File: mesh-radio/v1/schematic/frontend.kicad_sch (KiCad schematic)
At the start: 51 parts, among them J4 U.FL-R-SMT-1(80), U11 QPA9510TR7, U12 SKY13330-397LF, U13 BGA7L1BN6E6327XTSA1

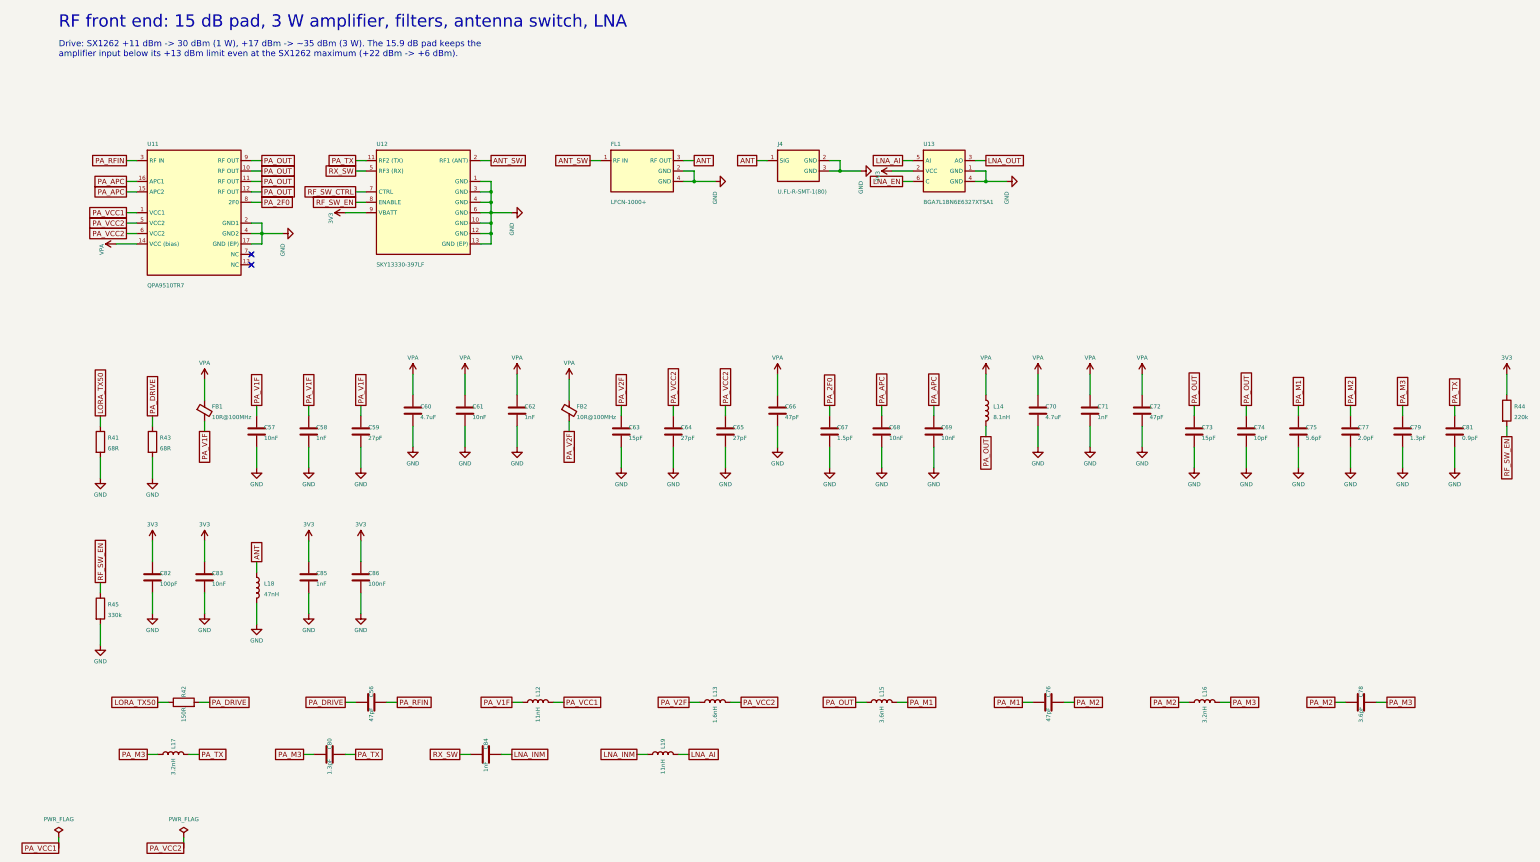
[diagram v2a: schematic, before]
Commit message: Mesh radio v1: LFCG-1000+ antenna filter; missing-antenna detector
Owner decisions of 19 Oct: keep 3 W with the heat fixes and a gap pad to
a metal enclosure, 6 layers, 300 mA charging, new parts at the designer's
judgement.  This commit, from sim/rf:
- FL1 LFCN-1000+ (1206) -> LFCG-1000+ (0805, 8 pads, Mini-Circuits case
  GE0805C-2: in 8, out 4): no stop-band re-entry at 5.5-10 GHz, where the
  3 W 6th-10th harmonics failed FCC's restricted-band limit;
- a reflected-wave detector: a printed line beside the ANT line
  terminated in 49.9 R, an Infineon BAT15-02EL, 1 nF and 100 k into
  P0.30/AIN6, so firmware can cut the amplifier within ~1 ms of a packet
  with no antenna (the antenna switch sees 109-160 % of its rating then);
- P0.31/AIN7 reads the charger's NTC (firmware's 0-45 C charging rule);
  the expansion header's IO3/IO4 give way (four spare pins remain).
ERC 0, netlist equals circuit.py, every pin and pad accounted for.

Co-Authored-By: Claude Opus 5.5 <noreply@anthropic.com>
Claude-Session: https://claude.ai/code/session_015TBB2ThqxHSgA8MkFosmn9
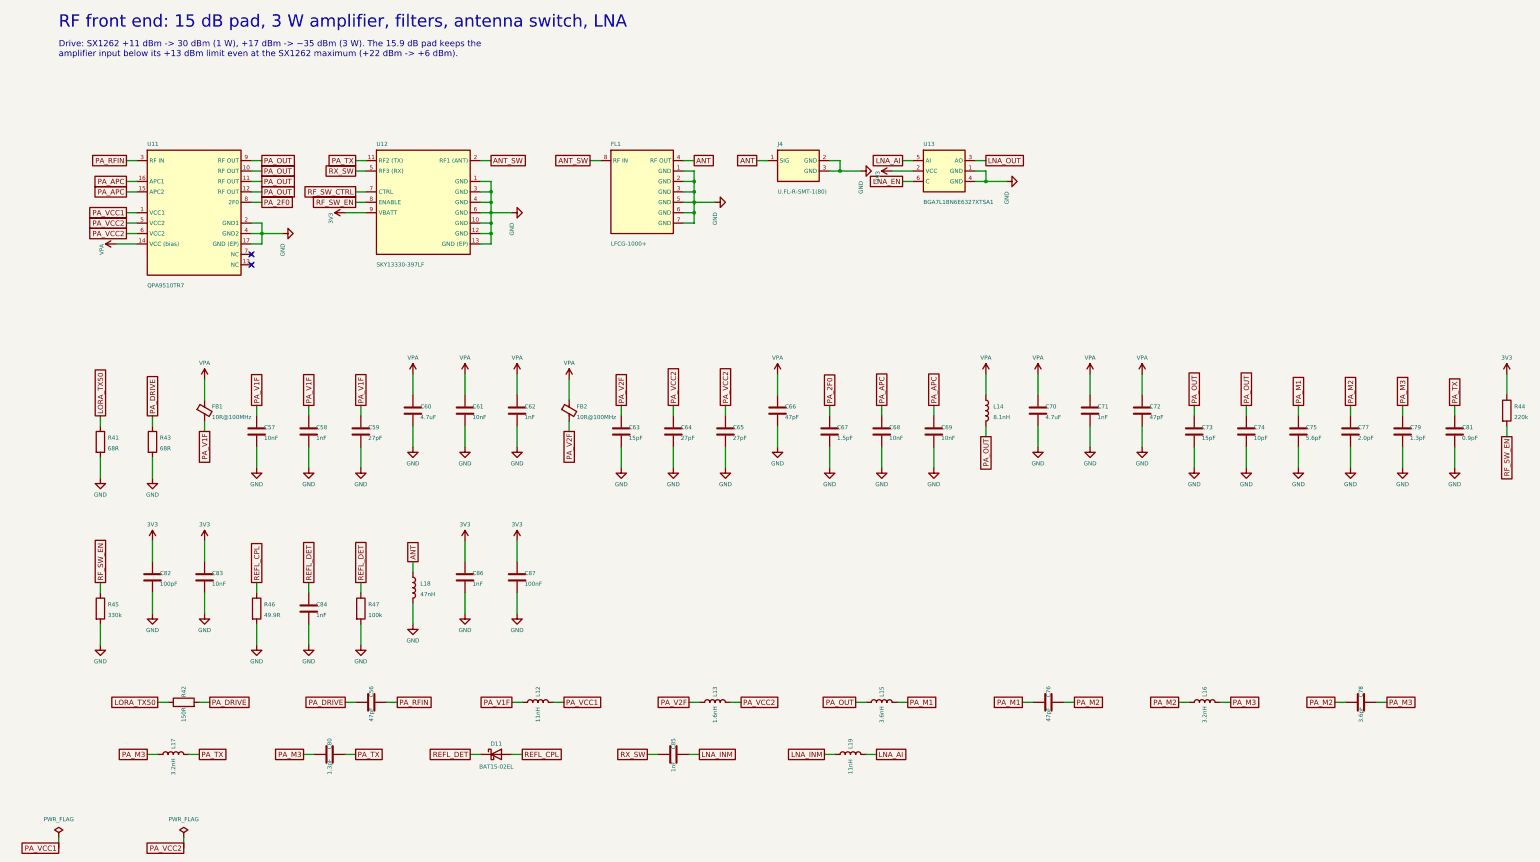
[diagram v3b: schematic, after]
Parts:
- added C87: 100nF, og:C_0402, symbol Device:C
- added D11: BAT15-02EL, og:TSLP-2-19_L1.0-W0.6-P0.65-RD, symbol og_device:D_Schottky_BAT15
- added R46: 49.9R, og:R_0402, symbol Device:R
- added R47: 100k, og:R_0402, symbol Device:R
- C77: DigiKey (none) -> 490-8124-1-ND
- C78: DigiKey (none) -> 490-8127-1-ND
- C81: DigiKey (none) -> 490-GQM1875C2ER90BB12DCT-ND
- C86: value 100nF -> 1nF; DigiKey 1276-1001-1-ND -> 490-3244-1-ND; LCSC C1525 -> C76947; MPN CL05B104KO5NNNC -> GRM1555C1H102JA01D; Manufacturer Samsung Electro-Mechanics -> Murata
- FL1: value LFCN-1000+ -> LFCG-1000+; footprint og:FILTER-SMD_1206-4P-L3.2-W1.6-L -> og:FILTER-SMD_8P-L2.0-W1.3-BL_LFCG-XX; symbol og:LFCN1000 -> og:LFCG1000; DigiKey 3157-LFCN-1000+CT-ND -> 3157-LFCG-1000+CT-ND; LCSC C879868 -> C4989745; MPN LFCN-1000+ -> LFCG-1000+
- L15: DigiKey (none) -> 490-16042-1-ND
- L16, L17: DigiKey (none) -> 490-16041-1-ND
- R41: DigiKey (none) -> 541-10549-1-ND
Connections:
- net 3V3: now also C87.1; no longer C85.1
- net ANT: now also FL1.4 (RF OUT); no longer FL1.3 (RF OUT)
- net ANT_SW: now also FL1.8 (RF IN); no longer FL1.1 (RF IN)
- net GND: now also C84.2, FL1.1 (GND), FL1.3 (GND), FL1.5 (GND), FL1.6 (GND), FL1.7 (GND), C87.2, R46.2, R47.2; no longer C85.2, FL1.4 (GND)
- net LNA_INM: now also C85.2; no longer C84.2
- net RX_SW: now also C85.1; no longer C84.1
- new net REFL_CPL: D11.2 (A), R46.1
- new net REFL_DET: C84.1, D11.1 (K), R47.1
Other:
- moved on the sheet: C84, C85, C86, L18, L19

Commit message: Mesh radio v1: power-path and firmware rework in progress (snapshot)
Co-Authored-By: Claude Opus 5.5 <noreply@anthropic.com>
Claude-Session: https://claude.ai/code/session_015TBB2ThqxHSgA8MkFosmn9
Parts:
- removed C86: 1nF, og:C_0402, symbol Device:C
- removed C87: 100nF, og:C_0402, symbol Device:C
- removed D11: BAT15-02EL, og:TSLP-2-19_L1.0-W0.6-P0.65-RD, symbol og_device:D_Schottky_BAT15
- removed R41, R43: 68R, og:R_0805, symbol Device:R
- removed R42: 150R, og:R_0805, symbol Device:R
- removed R44: 220k, og:R_0402, symbol Device:R
- removed R45: 330k, og:R_0402, symbol Device:R
- removed U13: BGA7L1BN6E6327XTSA1, og:TSNP-6_L1.1-W0.7-P0.40-BL, symbol og:BGA7L1BN6
- added C54: 47pF, og:C_0402, symbol Device:C
- added C55: 10nF, og:C_0402, symbol Device:C
- added D8: BAT15-02EL, og:TSLP-2-19_L1.0-W0.6-P0.65-RD, symbol og_device:D_Schottky_BAT15
- added R48: 68R, og:R_0805, symbol Device:R
- added R49: 220k, og:R_0402, symbol Device:R
- added R50: 330k, og:R_0402, symbol Device:R
- added R51: 49.9R, og:R_0402, symbol Device:R
- added R52: 100k, og:R_0402, symbol Device:R
- added U10: QPA9510TR7, og:QFN-16_3x3_QPA9510, symbol og:QPA9510
- C56: value 47pF -> 1nF; DigiKey 490-14446-1-ND -> 490-3244-1-ND; LCSC C161322 -> C76947; MPN GJM1555C1H470JB01D -> GRM1555C1H102JA01D
- C57: value 10nF -> 27pF; DigiKey 1276-1028-1-ND -> 490-17672-1-ND; LCSC C15195 -> C88884; MPN CL05B103KB5NNNC -> GJM1555C1H270JB01D; Manufacturer Samsung Electro-Mechanics -> Murata
- C58: value 1nF -> 4.7uF; footprint og:C_0402 -> og:C_0603; DigiKey 490-3244-1-ND -> 1276-1044-1-ND; LCSC C76947 -> C1705; MPN GRM1555C1H102JA01D -> CL10A475KP8NNNC; Manufacturer Murata -> Samsung Electro-Mechanics
- C59: value 27pF -> 10nF; DigiKey 490-17672-1-ND -> 1276-1028-1-ND; LCSC C88884 -> C15195; MPN GJM1555C1H270JB01D -> CL05B103KB5NNNC; Manufacturer Murata -> Samsung Electro-Mechanics
- C60: value 4.7uF -> 1nF; footprint og:C_0603 -> og:C_0402; DigiKey 1276-1044-1-ND -> 490-3244-1-ND; LCSC C1705 -> C76947; MPN CL10A475KP8NNNC -> GRM1555C1H102JA01D; Manufacturer Samsung Electro-Mechanics -> Murata
- C61: value 10nF -> 15pF; DigiKey 1276-1028-1-ND -> 490-3117-1-ND; LCSC C15195 -> C88877; MPN CL05B103KB5NNNC -> GJM1555C1H150JB01D; Manufacturer Samsung Electro-Mechanics -> Murata
- C62: value 1nF -> 27pF; DigiKey 490-3244-1-ND -> 490-17672-1-ND; LCSC C76947 -> C88884; MPN GRM1555C1H102JA01D -> GJM1555C1H270JB01D
- C63: value 15pF -> 27pF; DigiKey 490-3117-1-ND -> 490-17672-1-ND; LCSC C88877 -> C88884; MPN GJM1555C1H150JB01D -> GJM1555C1H270JB01D
- C64: value 27pF -> 47pF; DigiKey 490-17672-1-ND -> 490-14446-1-ND; LCSC C88884 -> C161322; MPN GJM1555C1H270JB01D -> GJM1555C1H470JB01D
- C65: value 27pF -> 1.5pF; DigiKey 490-17672-1-ND -> 490-8087-1-ND; LCSC C88884 -> C76900; MPN GJM1555C1H270JB01D -> GJM1555C1H1R5BB01D
- C66: value 47pF -> 10nF; DigiKey 490-14446-1-ND -> 1276-1028-1-ND; LCSC C161322 -> C15195; MPN GJM1555C1H470JB01D -> CL05B103KB5NNNC; Manufacturer Murata -> Samsung Electro-Mechanics
- C67: value 1.5pF -> 10nF; DigiKey 490-8087-1-ND -> 1276-1028-1-ND; LCSC C76900 -> C15195; MPN GJM1555C1H1R5BB01D -> CL05B103KB5NNNC; Manufacturer Murata -> Samsung Electro-Mechanics
- C68: value 10nF -> 4.7uF; footprint og:C_0402 -> og:C_0603; DigiKey 1276-1028-1-ND -> 1276-1044-1-ND; LCSC C15195 -> C1705; MPN CL05B103KB5NNNC -> CL10A475KP8NNNC
- C69, C83: value 10nF -> 1nF; DigiKey 1276-1028-1-ND -> 490-3244-1-ND; LCSC C15195 -> C76947; MPN CL05B103KB5NNNC -> GRM1555C1H102JA01D; Manufacturer Samsung Electro-Mechanics -> Murata
- C70: value 4.7uF -> 47pF; footprint og:C_0603 -> og:C_0402; DigiKey 1276-1044-1-ND -> 490-14446-1-ND; LCSC C1705 -> C161322; MPN CL10A475KP8NNNC -> GJM1555C1H470JB01D; Manufacturer Samsung Electro-Mechanics -> Murata
- C71: value 1nF -> 15pF; footprint og:C_0402 -> og:C_0603; DigiKey 490-3244-1-ND -> 490-14794-1-ND; LCSC C76947 -> C2181572; MPN GRM1555C1H102JA01D -> GQM1875C2E150JB12D
- C72: value 47pF -> 10pF; footprint og:C_0402 -> og:C_0603; DigiKey 490-14446-1-ND -> 490-6086-1-ND; LCSC C161322 -> C882554; MPN GJM1555C1H470JB01D -> GQM1875C2E100JB12D
- C73: value 15pF -> 5.6pF; DigiKey 490-14794-1-ND -> 490-7162-1-ND; LCSC C2181572 -> C2171689; MPN GQM1875C2E150JB12D -> GQM1875C2E5R6CB12D
- C74: value 10pF -> 47pF; DigiKey 490-6086-1-ND -> 490-5900-1-ND; LCSC C882554 -> C882552; MPN GQM1875C2E100JB12D -> GQM1875C2E470JB12D
- C75: value 5.6pF -> 2.0pF; DigiKey 490-7162-1-ND -> 490-8124-1-ND; LCSC C2171689 -> C6867410; MPN GQM1875C2E5R6CB12D -> GQM1875C2E2R0BB12D
- C76: value 47pF -> 3.6pF; DigiKey 490-5900-1-ND -> 490-8127-1-ND; LCSC C882552 -> C2178747; MPN GQM1875C2E470JB12D -> GQM1875C2E3R6BB12D
- C77: value 2.0pF -> 1.3pF; DigiKey 490-8124-1-ND -> (none); LCSC C6867410 -> C3901219; MPN GQM1875C2E2R0BB12D -> GQM1875C2E1R3BB12D
- C78: value 3.6pF -> 1.3pF; DigiKey 490-8127-1-ND -> (none); LCSC C2178747 -> C3901219; MPN GQM1875C2E3R6BB12D -> GQM1875C2E1R3BB12D
- C79: value 1.3pF -> 0.9pF; DigiKey (none) -> 490-GQM1875C2ER90BB12DCT-ND; LCSC C3901219 -> C1865143; MPN GQM1875C2E1R3BB12D -> GQM1875C2ER90BB12D
- C80: value 1.3pF -> 100pF; footprint og:C_0603 -> og:C_0402; DigiKey (none) -> 490-5922-1-ND; LCSC C3901219 -> C77177; MPN GQM1875C2E1R3BB12D -> GRM1555C1H101JA01D
- C81: value 0.9pF -> 10nF; footprint og:C_0603 -> og:C_0402; DigiKey 490-GQM1875C2ER90BB12DCT-ND -> 1276-1028-1-ND; LCSC C1865143 -> C15195; MPN GQM1875C2ER90BB12D -> CL05B103KB5NNNC; Manufacturer Murata -> Samsung Electro-Mechanics
- C82: value 100pF -> 1nF; DigiKey 490-5922-1-ND -> 490-3244-1-ND; LCSC C77177 -> C76947; MPN GRM1555C1H101JA01D -> GRM1555C1H102JA01D
- C85: value 1nF -> 100nF; DigiKey 490-3244-1-ND -> 1276-1001-1-ND; LCSC C76947 -> C1525; MPN GRM1555C1H102JA01D -> CL05B104KO5NNNC; Manufacturer Murata -> Samsung Electro-Mechanics
- R46: value 49.9R -> 68R; footprint og:R_0402 -> og:R_0805; DigiKey 311-49.9LRCT-ND -> 541-10549-1-ND; LCSC C87044 -> C2114866; MPN RC0402FR-0749R9L -> RCS080568R0FKEA; Manufacturer Yageo -> Vishay Dale
- R47: value 100k -> 150R; footprint og:R_0402 -> og:R_0805; DigiKey 311-100KLRCT-ND -> 311-150CRCT-ND; LCSC C60491 -> C114523; MPN RC0402FR-07100KL -> RC0805FR-07150RL
- U11: value QPA9510TR7 -> SKY13330-397LF; footprint og:QFN-16_3x3_QPA9510 -> og:QFN-12_L2.0-W2.0-P0.50-BL-EP0.8; symbol og:QPA9510 -> og:SKY13330; DigiKey 2312-QPA9510TR7CT-ND -> 863-1643-1-ND; LCSC C52059849 -> C2654715; MPN QPA9510TR7 -> SKY13330-397LF; Manufacturer Qorvo -> Skyworks Solutions
- U12: value SKY13330-397LF -> BGA7L1BN6E6327XTSA1; footprint og:QFN-12_L2.0-W2.0-P0.50-BL-EP0.8 -> og:TSNP-6_L1.1-W0.7-P0.40-BL; symbol og:SKY13330 -> og:BGA7L1BN6; DigiKey 863-1643-1-ND -> BGA7L1BN6E6327XTSA1CT-ND; LCSC C2654715 -> C534173; MPN SKY13330-397LF -> BGA7L1BN6E6327XTSA1; Manufacturer Skyworks Solutions -> Infineon Technologies
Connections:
- net 3V3: now also C80.1, C81.1, C84.1, C85.1, U11.9 (VBATT), U12.2 (VCC), R49.1; no longer C82.1, C83.1, U12.9 (VBATT)
- net ANT_SW: now also U11.2 (RF1 (ANT)); no longer U12.2 (RF1 (ANT))
- net GND: now also C56.2, C80.2, C85.2, U11.1 (GND), U11.10 (GND), U11.12 (GND), U11.13 (GND (EP)), U11.3 (GND), U11.6 (GND), C55.2, R48.2, R50.2, R51.2, R52.2, U10.17 (GND (EP)), U10.2 (GND1), U10.4 (GND2); no longer C74.2, C83.2, R47.2, U11.17 (GND (EP)), U11.2 (GND1), U12.10 (GND), U12.12 (GND), U12.13 (GND (EP)), U12.3 (GND), U12.6 (GND)
- net LNA_AI: now also U12.5 (AI)
- net LNA_EN: now also U12.6 (C)
- net LNA_INM: now also C83.2; no longer C85.2
- net LNA_OUT: now also U12.3 (AO)
- net LORA_TX50: now also R46.1, R47.1
- net PA_2F0: now also C65.1, U10.8 (2F0); no longer C67.1, U11.8 (2F0)
- net PA_APC: now also C66.1, C67.1, U10.15 (APC2), U10.16 (APC1); no longer C68.1, C69.1, U11.15 (APC2), U11.16 (APC1)
- net PA_DRIVE: now also R47.2, C54.1, R48.1; no longer C56.1
- net PA_M1: now also C73.1, C74.1; no longer C75.1, C76.1
- net PA_M2: now also C74.2, C75.1, C76.1; no longer C76.2, C77.1, C78.1
- net PA_M3: now also C76.2, C77.1, C78.1; no longer C78.2, C79.1, C80.1
- net PA_OUT: now also C71.1, C72.1, U10.10 (RF OUT), U10.11 (RF OUT), U10.12 (RF OUT), U10.9 (RF OUT); no longer C73.1, C74.1, U11.10 (RF OUT), U11.11 (RF OUT), U11.12 (RF OUT), U11.9 (RF OUT)
- net PA_RFIN: now also C54.2, U10.3 (RF IN); no longer C56.2, U11.3 (RF IN)
- net PA_TX: now also C78.2, C79.1, U11.11 (RF2 (TX)); no longer C80.2, C81.1, U12.11 (RF2 (TX))
- net PA_V1F: now also C56.1, C55.1; no longer C58.1, C59.1
- net PA_V2F: now also C61.1; no longer C63.1
- net PA_VCC1: now also U10.1 (VCC1); no longer U11.1 (VCC1)
- net PA_VCC2: now also C62.1, C63.1, U10.5 (VCC2), U10.6 (VCC2); no longer C64.1, C65.1, U11.5 (VCC2), U11.6 (VCC2)
- net REFL_CPL: now also D8.2 (A), R51.1; no longer R46.1
- net REFL_DET: now also C82.1, D8.1 (K), R52.1; no longer C84.1, R47.1
- net RF_SW_CTRL: now also U11.7 (CTRL); no longer U12.7 (CTRL)
- net RF_SW_EN: now also U11.8 (ENABLE), R49.2, R50.1; no longer U12.8 (ENABLE)
- net RX_SW: now also C83.1, U11.5 (RF3 (RX)); no longer C85.1, U12.5 (RF3 (RX))
- net VPA: now also C58.1, C59.1, C64.1, C68.1, C69.1, U10.14 (VCC (bias)); no longer C61.1, C62.1, C66.1, C71.1, C72.1, U11.14 (VCC (bias))
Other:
- moved on the sheet: C56, C57, C58, C59, C60, C61, C62, C63, C64, C65, C66, C67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

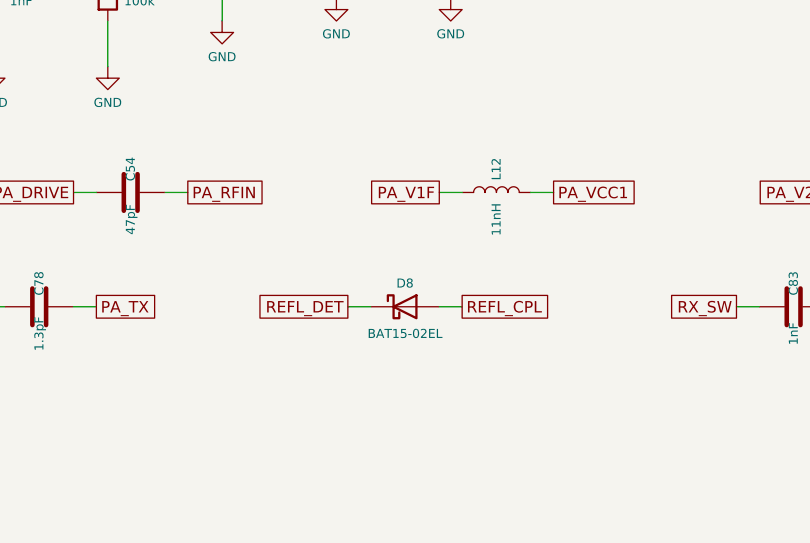
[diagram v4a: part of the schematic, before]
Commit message: Mesh Radio v1 schematic: regenerated (gate clamp, NTC part); ERC 0, netlist equal
Co-Authored-By: Claude Opus 5.5 <noreply@anthropic.com>
Claude-Session: https://claude.ai/code/session_015TBB2ThqxHSgA8MkFosmn9
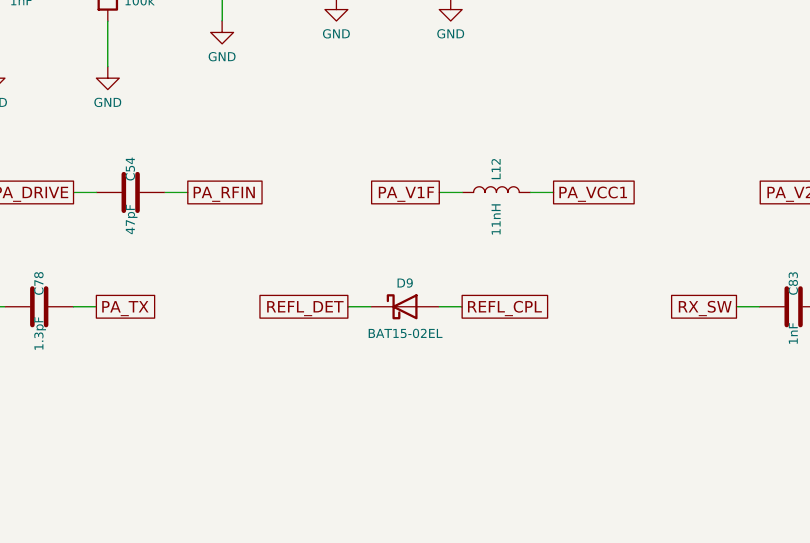
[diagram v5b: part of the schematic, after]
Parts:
- removed D8: BAT15-02EL, og:TSLP-2-19_L1.0-W0.6-P0.65-RD, symbol og_device:D_Schottky_BAT15
- added D9: BAT15-02EL, og:TSLP-2-19_L1.0-W0.6-P0.65-RD, symbol og_device:D_Schottky_BAT15
- C77, C78: DigiKey (none) -> 490-GQM1875C2E1R3BB12DCT-ND
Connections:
- net REFL_CPL: now also D9.2 (A)
- net REFL_DET: now also D9.1 (K)
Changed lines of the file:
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@@
 			)
 		)
+		(property "DigiKey" "490-GQM1875C2E1R3BB12DCT-ND"
+			(at 342.9 114.3 0)
+			(effects
+				(font
+					(size 1.27 1.27)
+				)
+				(hide yes)
+			)
+		)
 		(property "LCSC" "C3901219"
 			(at 342.9 114.3 0)
@@
 			)
 		)
+		(property "DigiKey" "490-GQM1875C2E1R3BB12DCT-ND"
+			(at 81.28 193.04 0)
+			(effects
+				(font
+					(size 1.27 1.27)
+				)
+				(hide yes)
+			)
+		)
 		(property "LCSC" "C3901219"
 			(at 81.28 193.04 0)
@@
 		(on_board yes)
 		(dnp no)
-		(property "Reference" "D8"
+		(property "Reference" "D9"
 			(at 121.92 190.44 0)
 			(effects
@@
 			(project "mesh-radio"
 				(path "/1e0df660-60b5-6ed0-6a2a-f5098e72ebfd/02e2910f-2b94-2e9a-4f24-7dfc00fa15a0"
-					(reference "D8")
+					(reference "D9")
 					(unit 1)
 				)

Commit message: Mesh Radio v1: ratio detector circuit and RF re-run in progress (snapshot)
Co-Authored-By: Claude Opus 5.5 <noreply@anthropic.com>
Claude-Session: https://claude.ai/code/session_015TBB2ThqxHSgA8MkFosmn9
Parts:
- added C99: 1nF, og:C_0402, symbol Device:C
- added D12: BAT6804WH6327XTSA1, og:SOT-323, symbol og:BAT68_04W
- added R74: 100k, og:R_0402, symbol Device:R
- D9: value BAT15-02EL -> BAT6804WH6327XTSA1; footprint og:TSLP-2-19_L1.0-W0.6-P0.65-RD -> og:SOT-323; symbol og_device:D_Schottky_BAT15 -> og:BAT68_04W; DigiKey BAT1502ELE6327XTMA1CT-ND -> BAT6804WH6327XTSA1CT-ND; LCSC C533619 -> C6129734; MPN BAT1502ELE6327XTMA1 -> BAT6804WH6327XTSA1
- R51: footprint og:R_0402 -> og:R_0805; DigiKey 311-49.9LRCT-ND -> 541-49.9TCT-ND; LCSC C87044 -> C4088942; MPN RC0402FR-0749R9L -> CRCW080549R9FKEAHP; Manufacturer Yageo -> Vishay Dale
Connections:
- net GND: now also C99.2, R74.2
- net REFL_CPL: now also D9.1 (A1), D12.1 (A1); no longer D9.2 (A)
- net REFL_DET: now also D9.2 (K2), D9.3 (K1/A2); no longer D9.1 (K)
- new net FWD_DET: C99.1, D12.2 (K2), D12.3 (K1/A2), R74.1
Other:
- moved on the sheet: C83, J4, L19, U12

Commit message: Mesh Radio v1: ratio antenna detector in the circuit (BAT68-04W pair, 0805 49.9 R)
Forward detector D12 (FWD_DET, P0.02/AIN0) at the coupled line's filter
end, a second 49.9 R (R75) at its U.FL end so the reflected copy does
not cancel the forward reading; BAT15 replaced by Infineon BAT68-04W
(8 V; BAT62 not stocked), 49.9 R by Vishay CRCW0805 pulse-proof.
PA_SRC_SYS on P1.09, GPS pin 5 pulled up to the GPS supply.
sim/rf study 8: fault if FWD_DET < Fmin(P,T) or REFL/FWD > R(P,T)
detects a missing antenna from 30 dBm, -40..85 C, every diode pairing.
Schematic regenerated: netlist equal, ERC 0.

Co-Authored-By: Claude Opus 5.5 <noreply@anthropic.com>
Claude-Session: https://claude.ai/code/session_015TBB2ThqxHSgA8MkFosmn9
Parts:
- added R75: 49.9R, og:R_0805, symbol Device:R
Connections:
- net GND: now also R75.2
- net REFL_CPL: now also R75.1
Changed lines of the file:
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@@
+	(symbol
+		(lib_id "Device:R")
+		(at 165.1 157.48 0)
+		(unit 1)
+		(exclude_from_sim no)
+		(in_bom yes)
+		(on_board yes)
+		(dnp no)
+		(property "Reference" "R75"
+			(at 166.9 156.48 0)
+			(effects
+				(font
+					(size 1 1)
+				)
+				(justify left)
+			)
+		)
+		(property "Value" "49.9R"
+			(at 166.9 159.08 0)
+			(effects
+				(font
+					(size 1 1)
+				)
+				(justify left)
+			)
+		)
+		(property "Footprint" "og:R_0805"
+			(at 165.1 157.48 0)
+			(effects
+				(font
+					(size 1.27 1.27)
+				)
+				(hide yes)
+			)
+		)
+		(property "MPN" "CRCW080549R9FKEAHP"
+			(at 165.1 157.48 0)
+			(effects
+				(font
+					(size 1.27 1.27)
+				)
+				(hide yes)
+			)
+		)
+		(property "Manufacturer" "Vishay Dale"
+			(at 165.1 157.48 0)
+			(effects
+				(font
+					(size 1.27 1.27)
+				)
+				(hide yes)
+			)
+		)
+		(property "DigiKey" "541-49.9TCT-ND"
+			(at 165.1 157.48 0)
+			(effects
+				(font
+					(size 1.27 1.27)
+				)
+				(hide yes)
+			)
+		)
+		(property "LCSC" "C4088942"
+			(at 165.1 157.48 0)
+			(effects
+				(font
+					(size 1.27 1.27)
+				)
+				(hide yes)
+			)
+		)
+		(property "Description" "Resistor 49.9R 1% 0.5 W pulse-proof 0805"
+			(at 165.1 157.48 0)
+			(effects
+				(font
+					(size 1.27 1.27)
+				)
+				(hide yes)
+			)
+		)
+		(instances
+			(project "mesh-radio"
+				(path "/1e0df660-60b5-6ed0-6a2a-f5098e72ebfd/02e2910f-2b94-2e9a-4f24-7dfc00fa15a0"
+					(reference "R75")
+					(unit 1)
+				)
+			)
+		)
+	)
+	(wire
+		(pts
+			(xy 165.1 153.67)
+			(xy 165.1 151.13)
+		)
+		(stroke
+			(width 0)
+			(type default)
+		)
+	)
+	(global_label "REFL_CPL"
+		(shape passive)
+		(at 165.1 151.13 90)
+		(fields_autoplaced yes)
+		(effects
+			(font
+				(size 1.27 1.27)
+			)
+			(justify left)
+		)
+		(property "Intersheetrefs" "${INTERSHEET_REFS}"
+			(at 165.1 151.13 0)
+			(effects
+				(font
+					(size 1.27 1.27)
+				)
+				(justify left)
+				(hide yes)
+			)
+		)
+	)
+	(wire
+		(pts
+			(xy 165.1 161.29)
+			(xy 165.1 166.37)
+		)
+		(stroke
+			(width 0)
+			(type default)
+		)
+	)
+	(symbol
+		(lib_id "power:GND")
+		(at 165.1 166.37 0)
+		(unit 1)
+		(exclude_from_sim no)
+		(in_bom no)
+		(on_board no)
+		(dnp no)
+		(property "Reference" "#PWRFRO059"
+			(at 165.1 163.17 0)
+			(effects
+				(font
+					(size 1 1)
+				)
+				(hide yes)
+			)
+		)
+		(property "Value" "GND"
+			(at 165.1 170.37 0)
+			(effects
+				(font
+					(size 1 1)
+				)
+			)
+		)
+		(instances
+			(project "mesh-radio"
+				(path "/1e0df660-60b5-6ed0-6a2a-f5098e72ebfd/02e2910f-2b94-2e9a-4f24-7dfc00fa15a0"
+					(reference "#PWRFRO059")
+					(unit 1)
+				)
+			)
+		)
+	)
 	(symbol
 		(lib_id "Device:R")
@@
 		(on_board no)
 		(dnp no)
-		(property "Reference" "#FLGFRO59"
+		(property "Reference" "#FLGFRO60"
 			(at 15.24 210.16 0)
 			(effects
@@
 			(project "mesh-radio"
 				(path "/1e0df660-60b5-6ed0-6a2a-f5098e72ebfd/02e2910f-2b94-2e9a-4f24-7dfc00fa15a0"
-					(reference "#FLGFRO59")
+					(reference "#FLGFRO60")
 					(unit 1)
 				)
@@
 		(on_board no)
 		(dnp no)
-		(property "Reference" "#FLGFRO60"
+		(property "Reference" "#FLGFRO61"
 			(at 45.72 210.16 0)
 			(effects
@@
 			(project "mesh-radio"
 				(path "/1e0df660-60b5-6ed0-6a2a-f5098e72ebfd/02e2910f-2b94-2e9a-4f24-7dfc00fa15a0"
-					(reference "#FLGFRO60")
+					(reference "#FLGFRO61")
 					(unit 1)
 				)
